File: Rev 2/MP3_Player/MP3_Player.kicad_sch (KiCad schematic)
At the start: 26 parts, among them J1 AudioJack3_SwitchT, M1 Haptic Feedback, Q1 BS170, SW1 Home, SW2 Back, SW3 Play/Pause, SW4 Power, SW5 Menu, SW6 Hold, U1 Wemos Lolin32 Lite

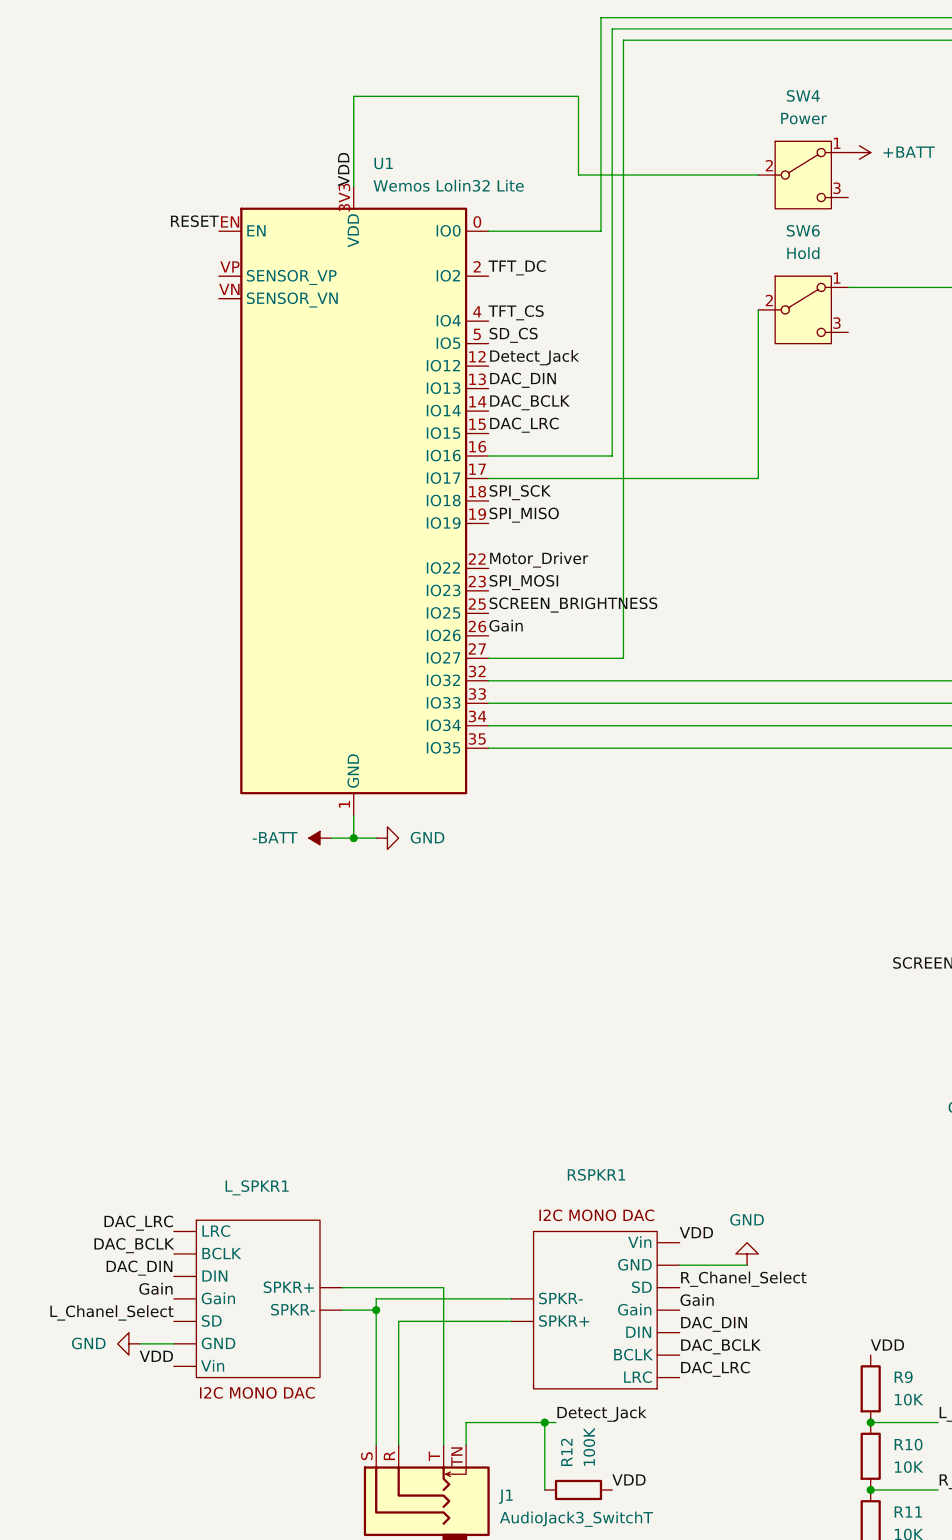
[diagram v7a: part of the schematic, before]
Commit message: Fixed Power Switch
-Fixed Wiring so power switch is interrupting the battery on its way to the battery charger
-Fixed Footprint linking issues
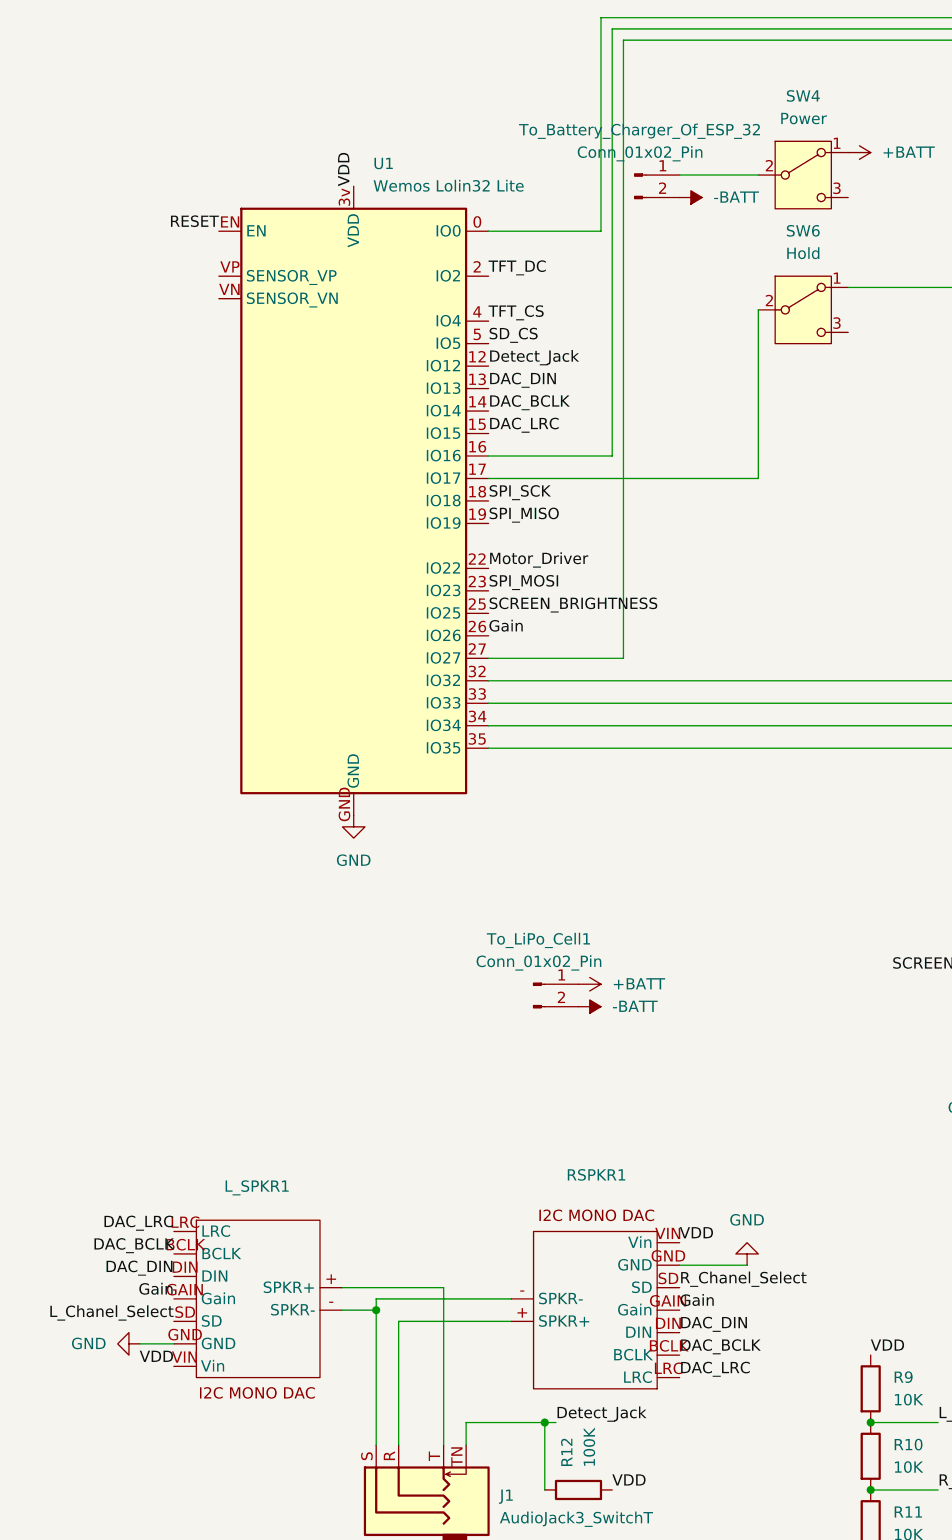
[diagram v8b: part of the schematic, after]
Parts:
- added To_Battery_Charger_Of_ESP_32, To_LiPo_Cell1: Conn_01x02_Pin, Connector_JST:JST_XA_B02B-XASK-1-A_1x02_P2.50mm_Vertical, symbol Connector:Conn_01x02_Pin
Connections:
- net +BATT: now also To_LiPo_Cell1.1 (Pin_1)
- net -BATT: now also To_Battery_Charger_Of_ESP_32.2 (Pin_2), To_LiPo_Cell1.2 (Pin_2); no longer L_SPKR1. (Vin), M1.2 (-), Primary Rotary Encoder1.C, R1.2, R2.2, R3.1, R4.1, R5.1, R6.1, R8.1, RSPKR1. (Vin), Screen&SDCardReader1.GND, U1.1 (GND), U1.39 (GND), U1.GND
- net DAC_BCLK: now also L_SPKR1.BCLK, RSPKR1.BCLK; no longer L_SPKR1. (Vin), RSPKR1. (Vin)
- net DAC_DIN: now also L_SPKR1.DIN, RSPKR1.DIN; no longer L_SPKR1. (Vin), RSPKR1. (Vin)
- net DAC_LRC: now also L_SPKR1.LRC, RSPKR1.LRC; no longer L_SPKR1. (Vin), RSPKR1. (Vin)
- net Gain: now also L_SPKR1.GAIN (Gain), RSPKR1.GAIN (Gain); no longer L_SPKR1. (Vin), RSPKR1. (Vin)
- net L_Chanel_Select: now also L_SPKR1.SD; no longer L_SPKR1. (Vin)
- net R_Chanel_Select: now also RSPKR1.SD; no longer RSPKR1. (Vin)
- net VDD: now also L_SPKR1.VIN (Vin), RSPKR1.VIN (Vin), U1.3v (VDD); no longer L_SPKR1. (Vin), RSPKR1. (Vin), SW4.2 (B), U1.3V3 (VDD)
- net at J1.T: now also L_SPKR1.+ (SPKR+); no longer L_SPKR1. (Vin)
- net at J1.R: now also RSPKR1.+ (SPKR+); no longer RSPKR1. (Vin)
- new net: J1.S, L_SPKR1.- (SPKR-), RSPKR1.- (SPKR-)
- new net: SW4.2 (B), To_Battery_Charger_Of_ESP_32.1 (Pin_1)
- new net GND: L_SPKR1.GND, M1.2 (-), Primary Rotary Encoder1.C, R1.2, R2.2, R3.1, R4.1, R5.1, R6.1, R8.1, RSPKR1.GND, Screen&SDCardReader1.GND, U1.GND
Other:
- moved on the sheet: U1
